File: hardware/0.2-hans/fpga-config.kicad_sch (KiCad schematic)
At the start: 28 parts, among them J2 JTAG, J5 USB_Type_C_2.0, Q500 BSS138, SW1 PTS810, U1 W25Q128JVPIQ, U2 ECP5U_25_CABGA256

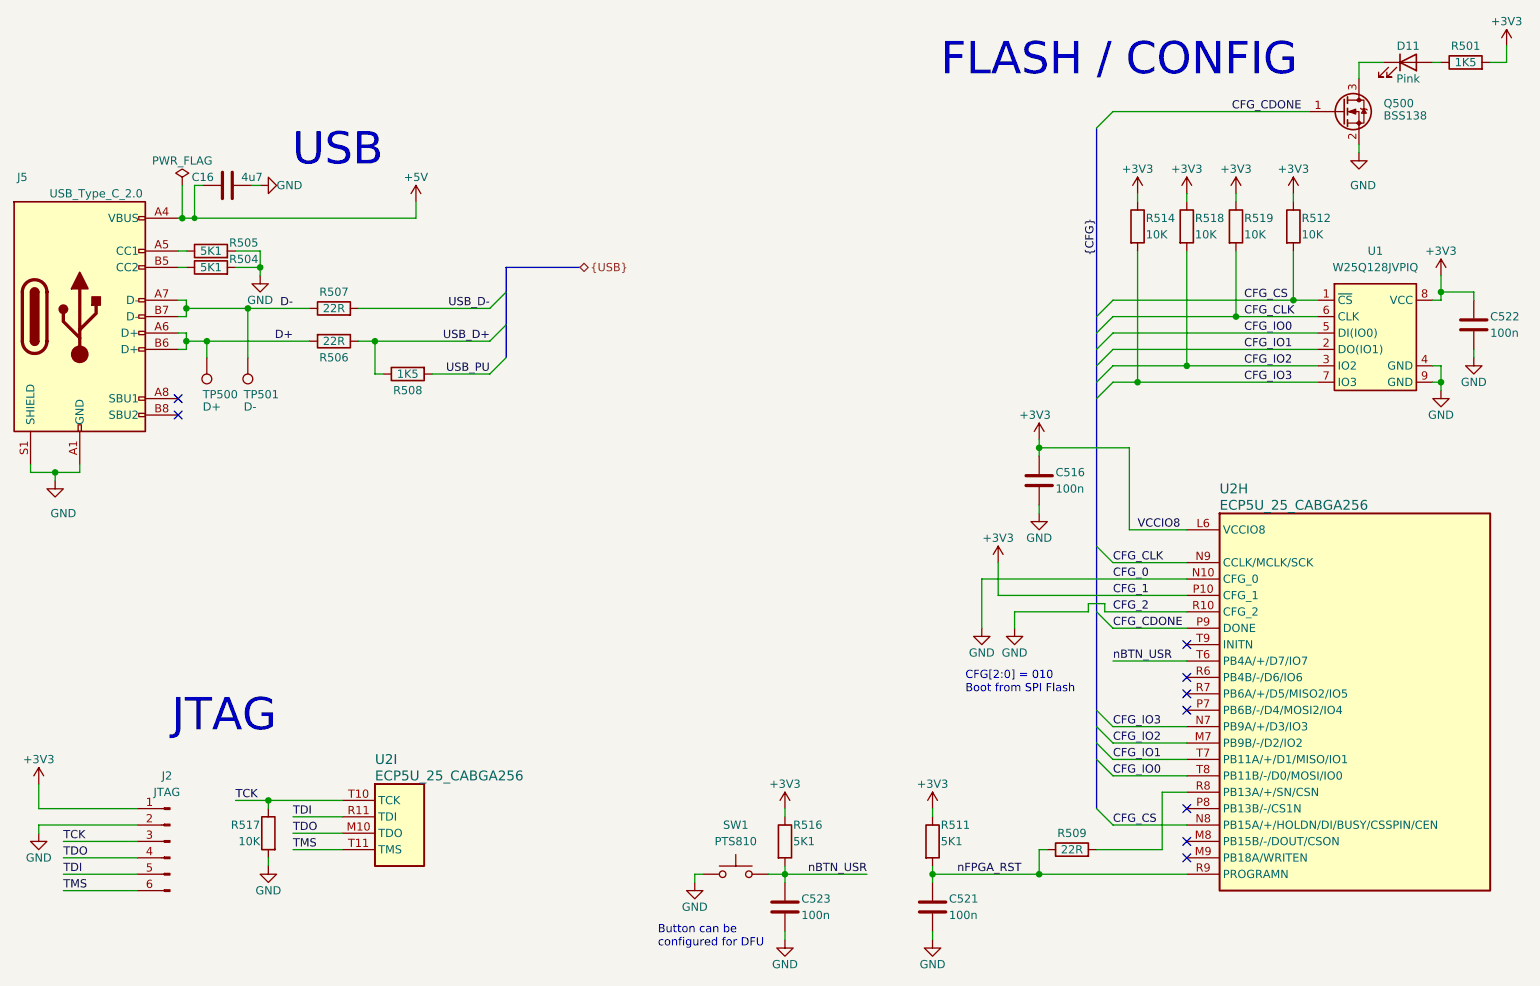
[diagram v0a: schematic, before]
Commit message: remove usb, add 5v
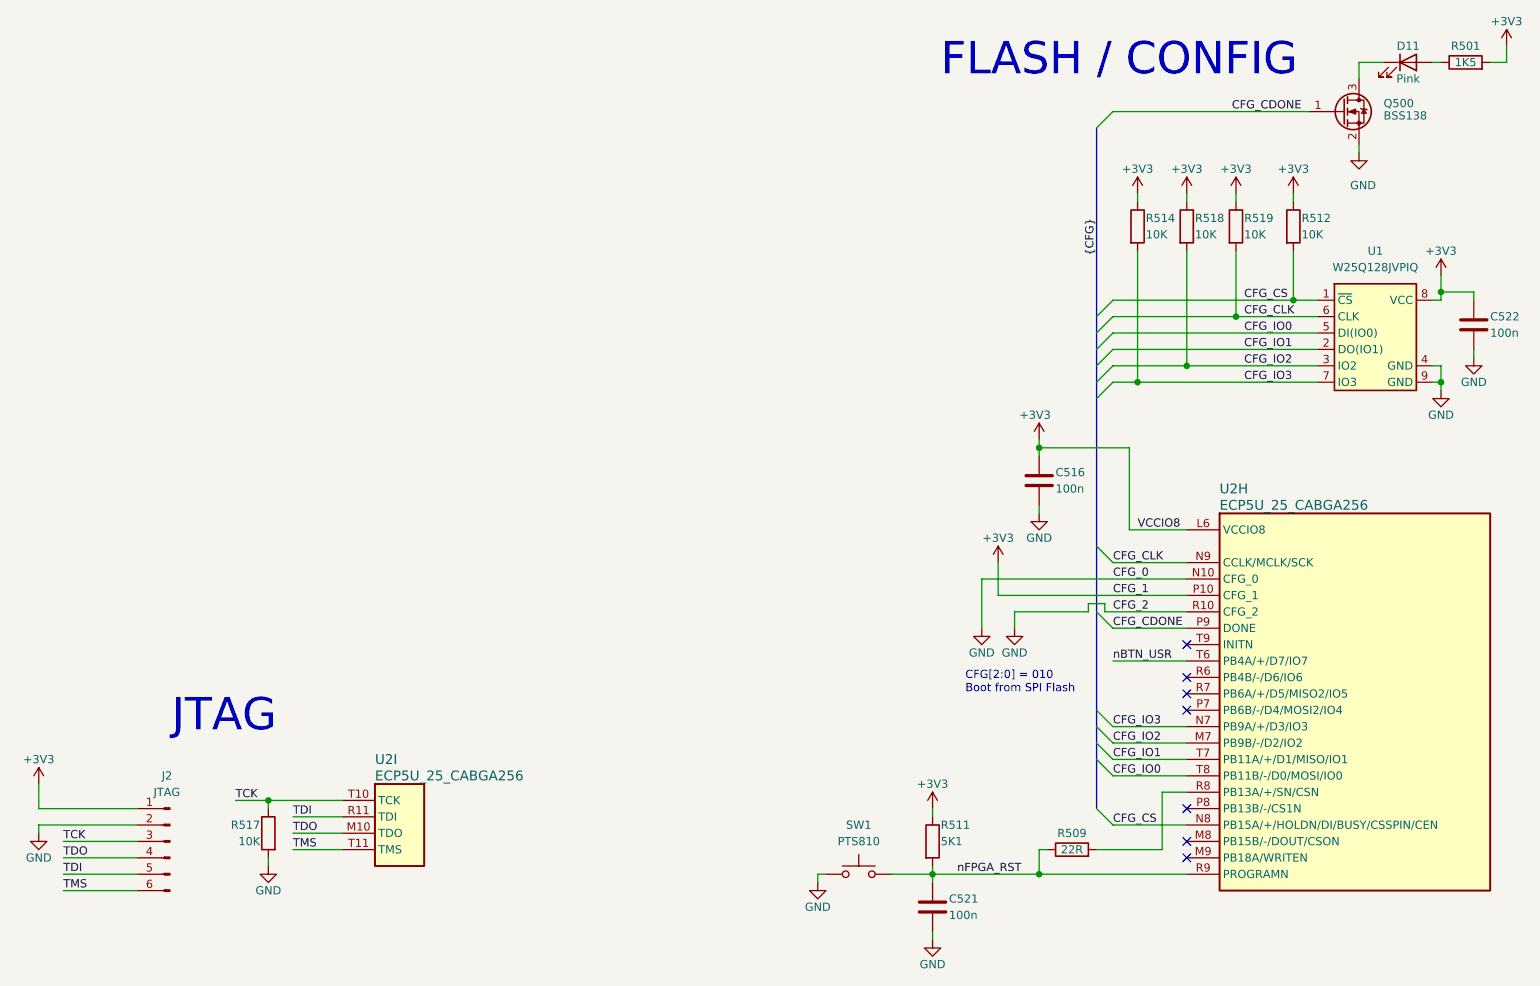
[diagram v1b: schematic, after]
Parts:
- removed C16: 4u7, Capacitor_SMD:C_0402_1005Metric, symbol Device:C
- removed C523: 100n, Capacitor_SMD:C_0402_1005Metric, symbol Device:C
- removed J5: USB_Type_C_2.0, josh-connectors:USB_C_Receptacle_HRO_TYPE-C-31-M-12, symbol Connector:USB_C_Receptacle_USB2.0
- removed R504, R505, R516: 5K1, Resistor_SMD:R_0402_1005Metric, symbol Device:R
- removed R506, R507: 22R, Resistor_SMD:R_0402_1005Metric, symbol Device:R
- removed R508: 1K5, Resistor_SMD:R_0402_1005Metric, symbol Device:R
- removed TP500: D+, TestPoint:TestPoint_Pad_D1.5mm, symbol Connector:TestPoint
- removed TP501: D-, TestPoint:TestPoint_Pad_D1.5mm, symbol Connector:TestPoint
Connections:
- net nBTN_USR: no longer SW1.2
- net nFPGA_RST: now also SW1.2
- no-connect marks 9 -> 7
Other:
- note removed: "Button can be configured for DFU"
- note removed: "USB"
- moved on the sheet: SW1
